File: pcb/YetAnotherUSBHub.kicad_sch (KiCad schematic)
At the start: 23 parts, among them J1 USB_A, J2 USB_A, J3 Micro_SD_Card, J4 USB_C_Receptacle_USB2.0_14P, J5 USB_C_Receptacle_USB2.0_14P, U2 GL823K-HCY04

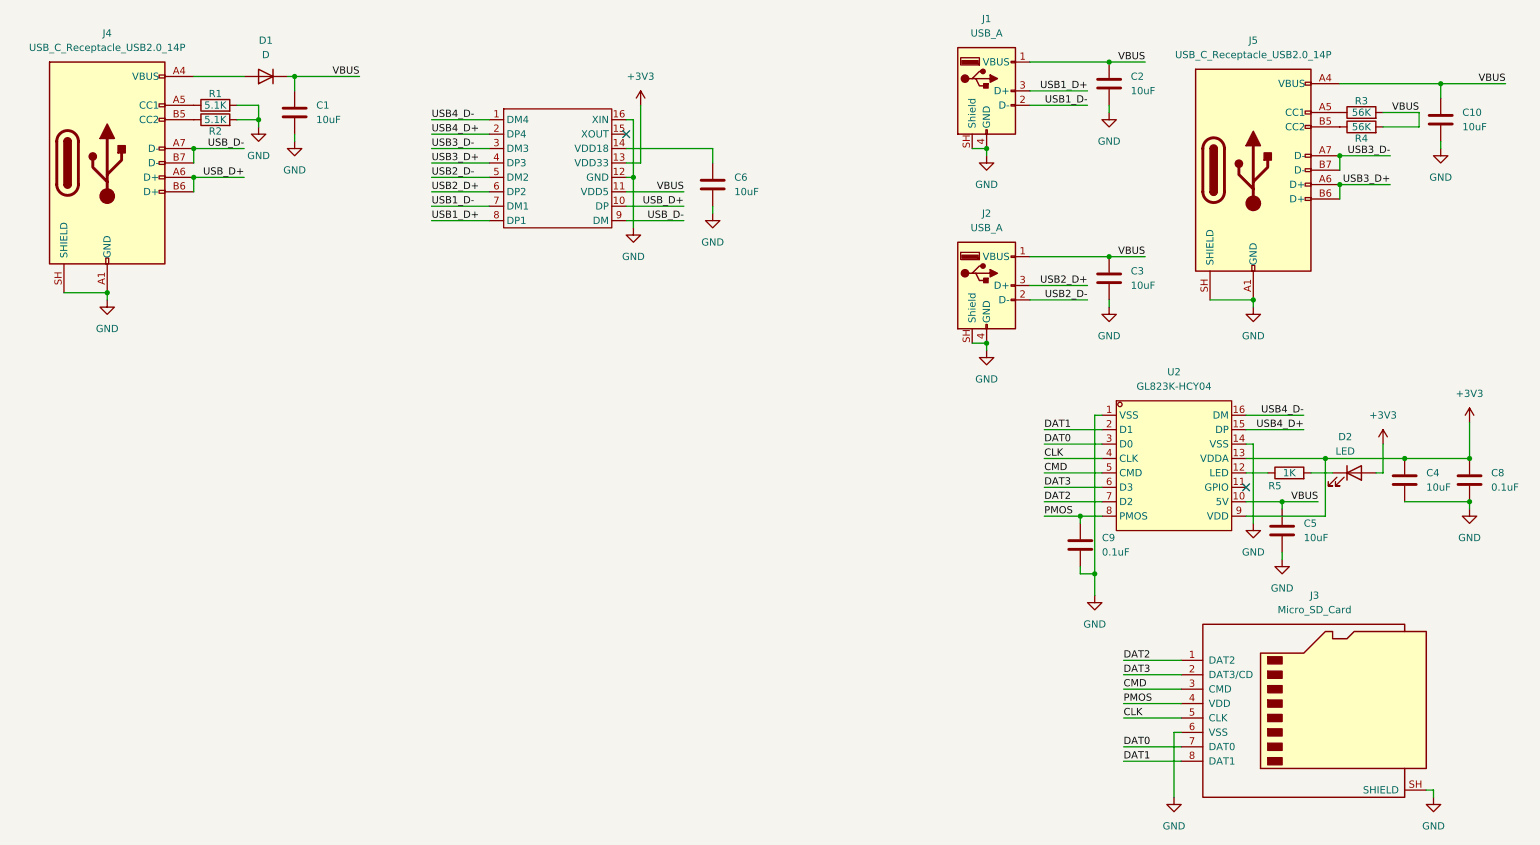
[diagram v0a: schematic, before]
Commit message: esd protection on pcb
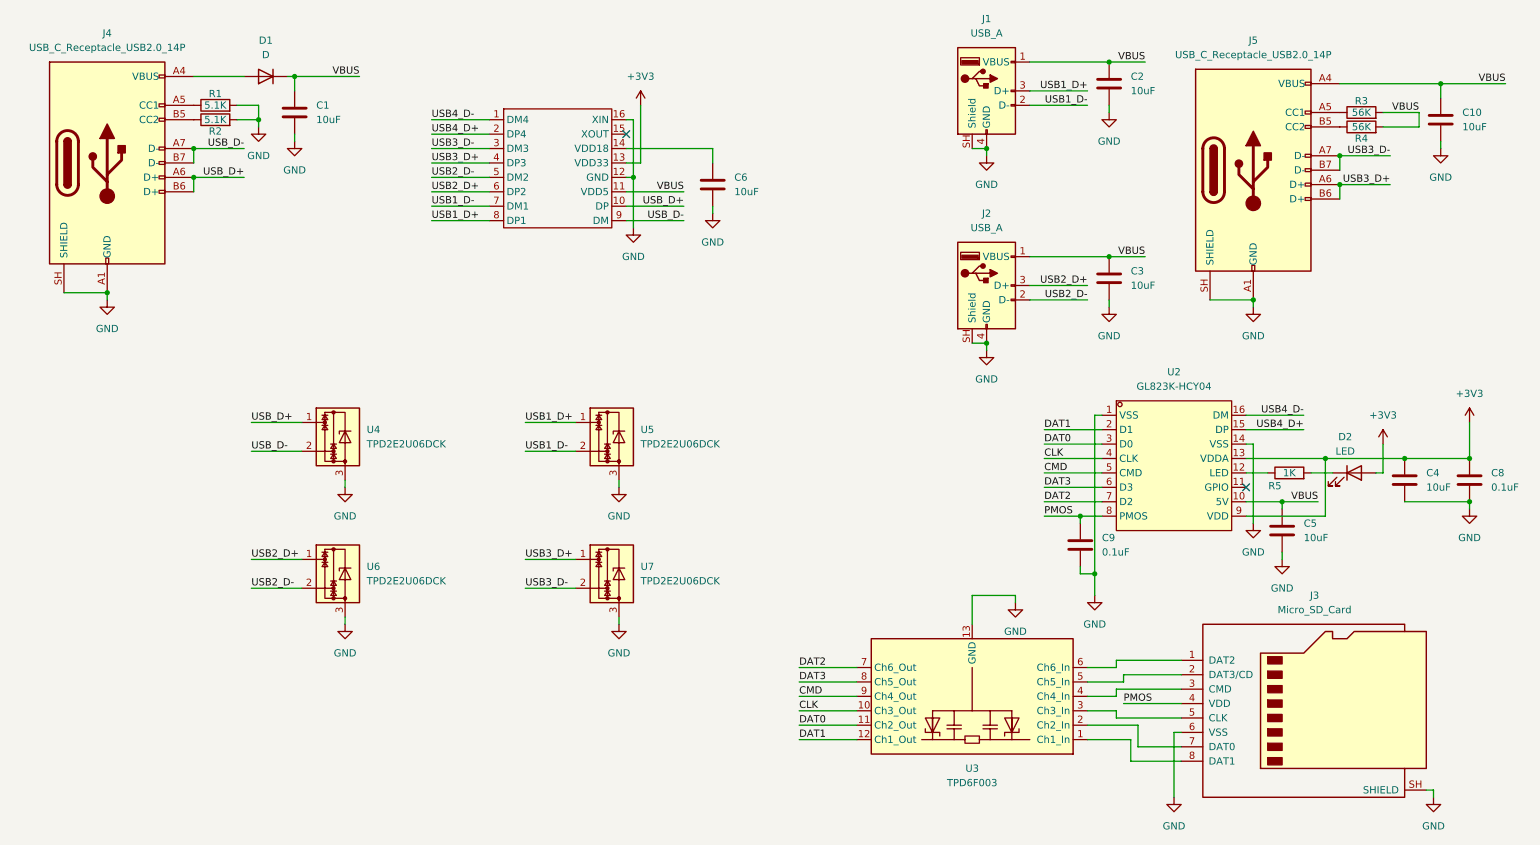
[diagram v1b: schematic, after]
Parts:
- added U3: TPD6F003, Package_SON:Texas_R-PWSON-N12_EP0.4x2mm, symbol Power_Protection:TPD6F003
- added U4, U5, U6, U7: TPD2E2U06DCK, Package_TO_SOT_SMD:SOT-323_SC-70, symbol Power_Protection:TPD2E2U06DCK
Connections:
- net CLK: now also U3.10 (Ch3_Out); no longer J3.5 (CLK)
- net CMD: now also U3.9 (Ch4_Out); no longer J3.3 (CMD)
- net DAT0: now also U3.11 (Ch2_Out); no longer J3.7 (DAT0)
- net DAT1: now also U3.12 (Ch1_Out); no longer J3.8 (DAT1)
- net DAT2: now also U3.7 (Ch6_Out); no longer J3.1 (DAT2)
- net DAT3: now also U3.8 (Ch5_Out); no longer J3.2 (DAT3/CD)
- net GND: now also U3.13 (GND), U4.3, U5.3, U6.3, U7.3
- net USB1_D+: now also U5.1
- net USB1_D-: now also U5.2
- net USB2_D+: now also U6.1
- net USB2_D-: now also U6.2
- net USB3_D+: now also U7.1
- net USB3_D-: now also U7.2
- net USB_D+: now also U4.1
- net USB_D-: now also U4.2
- new net: J3.1 (DAT2), U3.6 (Ch6_In)
- new net: J3.2 (DAT3/CD), U3.5 (Ch5_In)
- new net: J3.3 (CMD), U3.4 (Ch4_In)
- new net: J3.5 (CLK), U3.3 (Ch3_In)
- new net: J3.7 (DAT0), U3.2 (Ch2_In)
- new net: J3.8 (DAT1), U3.1 (Ch1_In)
